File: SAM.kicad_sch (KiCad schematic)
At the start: 27 parts, among them J1 Bus_Apple_II_Card_Side, J2 Conn_01x02_Pin, U1 DAC08, U2 L7805, U3 LM380N, U4 74LS273

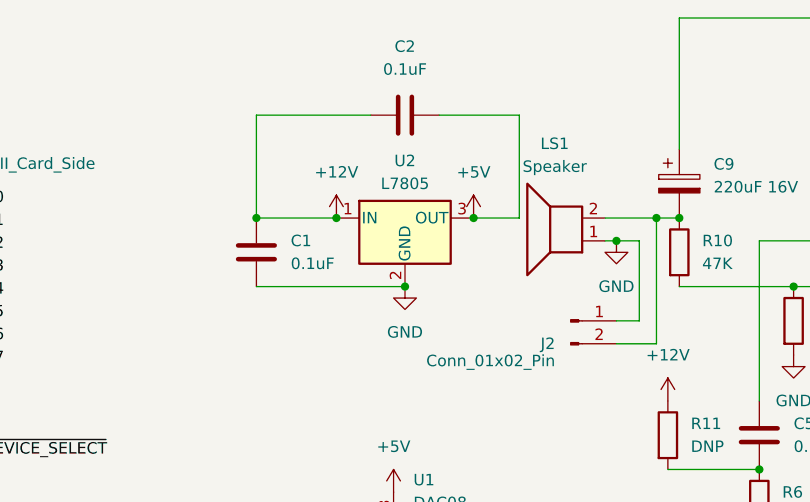
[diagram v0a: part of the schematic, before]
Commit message: change 7805 to 78L05
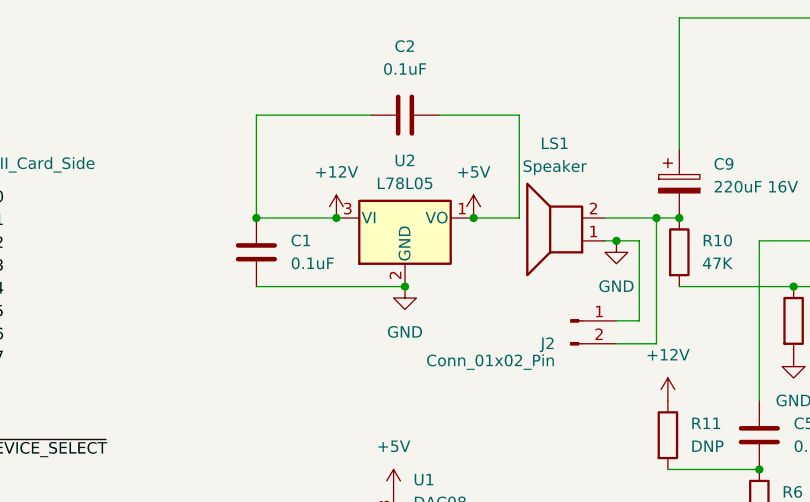
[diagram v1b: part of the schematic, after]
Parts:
- U2: value L7805 -> L78L05; footprint Package_TO_SOT_THT:TO-92L_Wide -> Package_TO_SOT_THT:TO-92_Inline; symbol Regulator_Linear:L7805 -> Regulator_Linear:L78L05_TO92
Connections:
- net +12V: now also U2.3 (VI); no longer U2.1 (IN)
- net +5V: now also U2.1 (VO); no longer U2.3 (OUT)
